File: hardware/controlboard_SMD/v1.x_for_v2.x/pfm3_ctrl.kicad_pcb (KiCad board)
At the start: 2 copper layers, 135 x 87 mm, 63 parts, among them J1 Conn_01x06, SW1 Push, SW10 Push, SW11 Push, SW12 Push, SW2 Push, SW3 Push, SW4 Push, SW5 Push, SW6 Push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

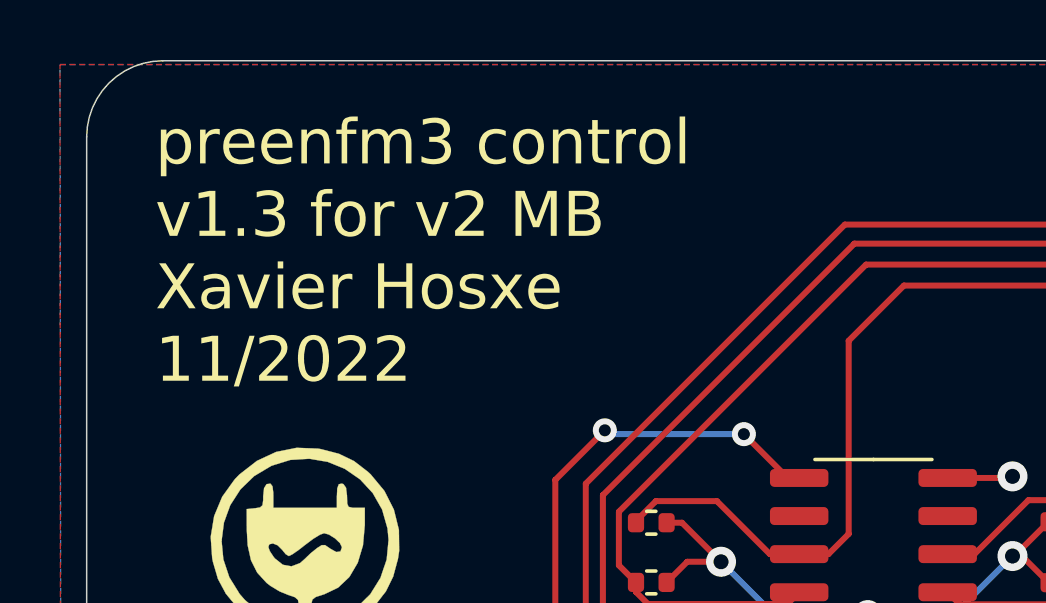
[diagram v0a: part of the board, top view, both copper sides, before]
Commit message: Small control board PCB modification: wider clearance around placement holes
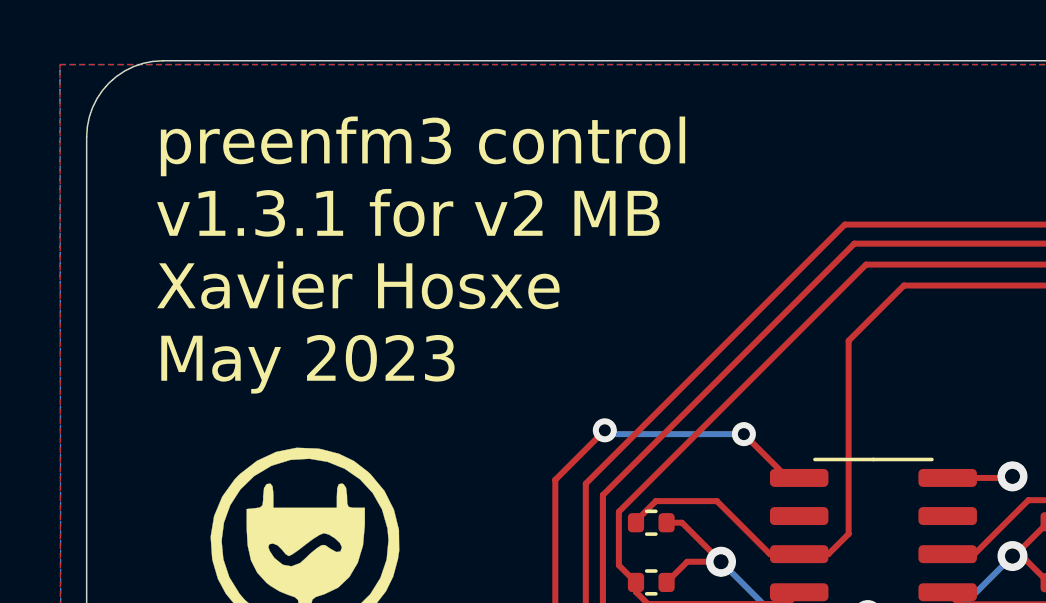
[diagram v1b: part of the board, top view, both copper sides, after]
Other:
- board text added: "preenfm3 control v1.3.1 for v2 MB Xavier Hosxe May 2023"
- board text removed: "preenfm3 control v1.3 for v2 MB Xavier Hosxe 11/2022"
